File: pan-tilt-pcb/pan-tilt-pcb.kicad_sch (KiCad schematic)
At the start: 23 parts, among them J1 Conn_01x03, J10 USB_C_Receptacle_USB2.0_14P, J2 NC5MAV, J3 NC5FAV, J4 Conn_01x03, J5 Conn_01x03, J6 Conn_01x03, J7 Conn_01x03, J8 Conn_01x12, J9 Conn_01x12, SW1 SW_Push, SW2 SW_Push

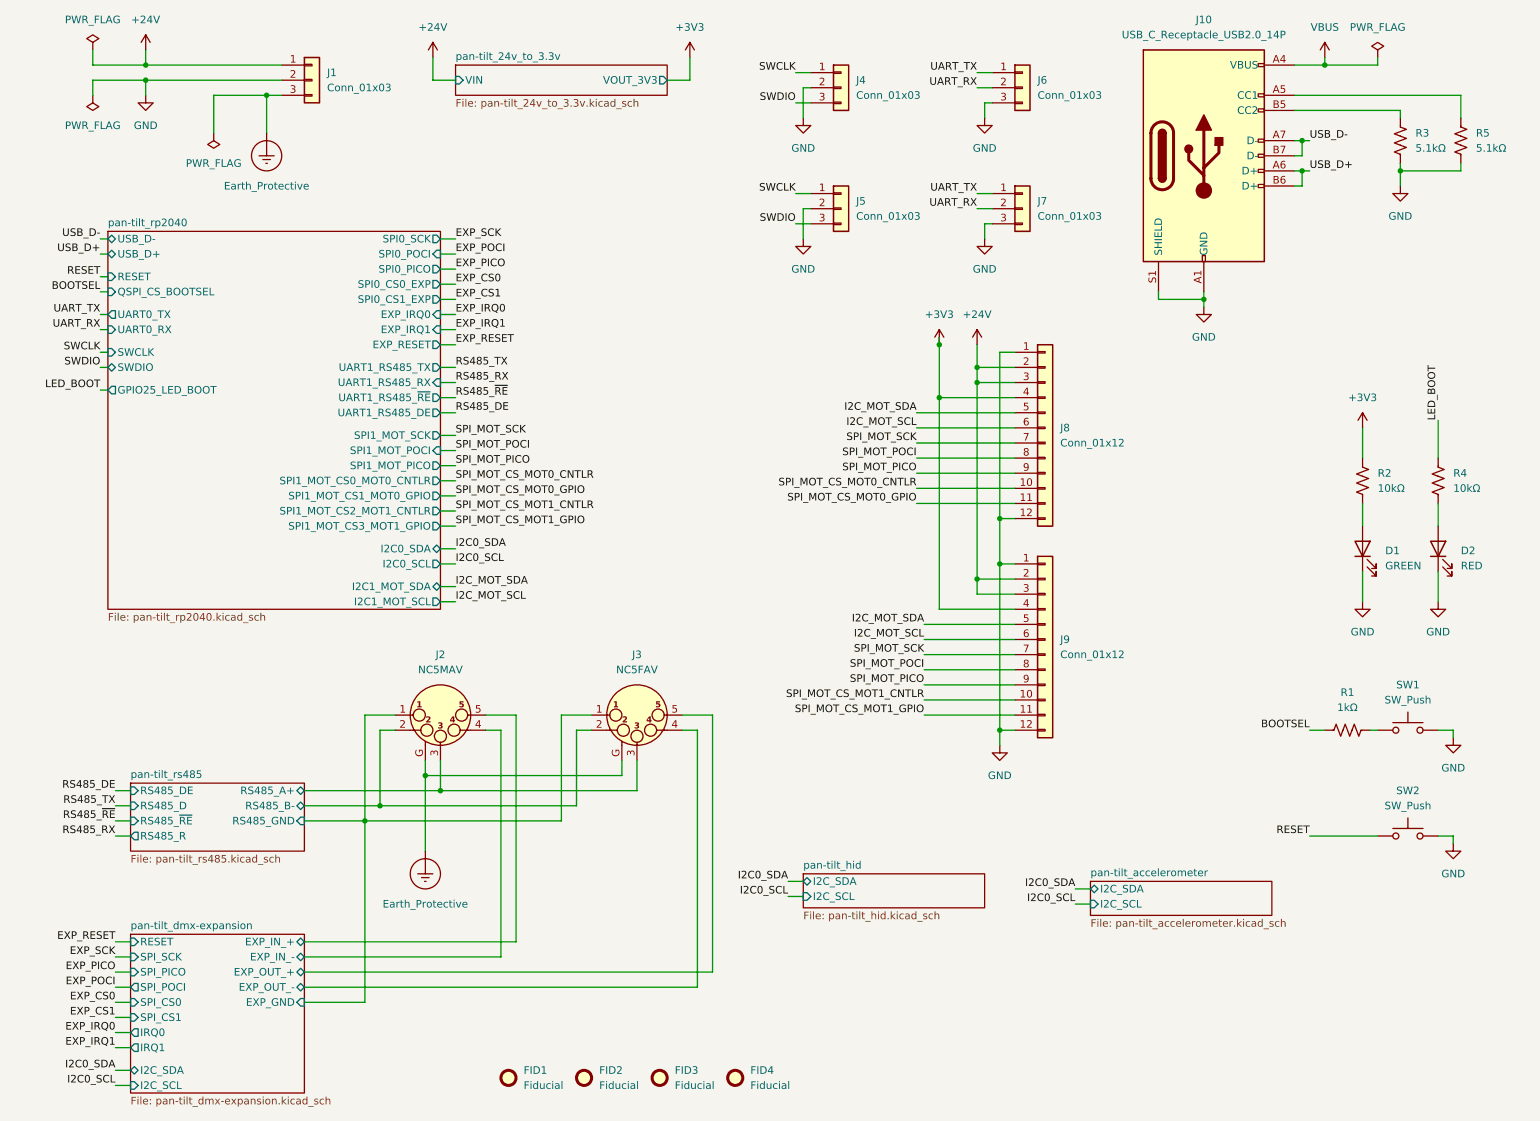
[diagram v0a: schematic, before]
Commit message: fix missing pieces, incorporate review feedback
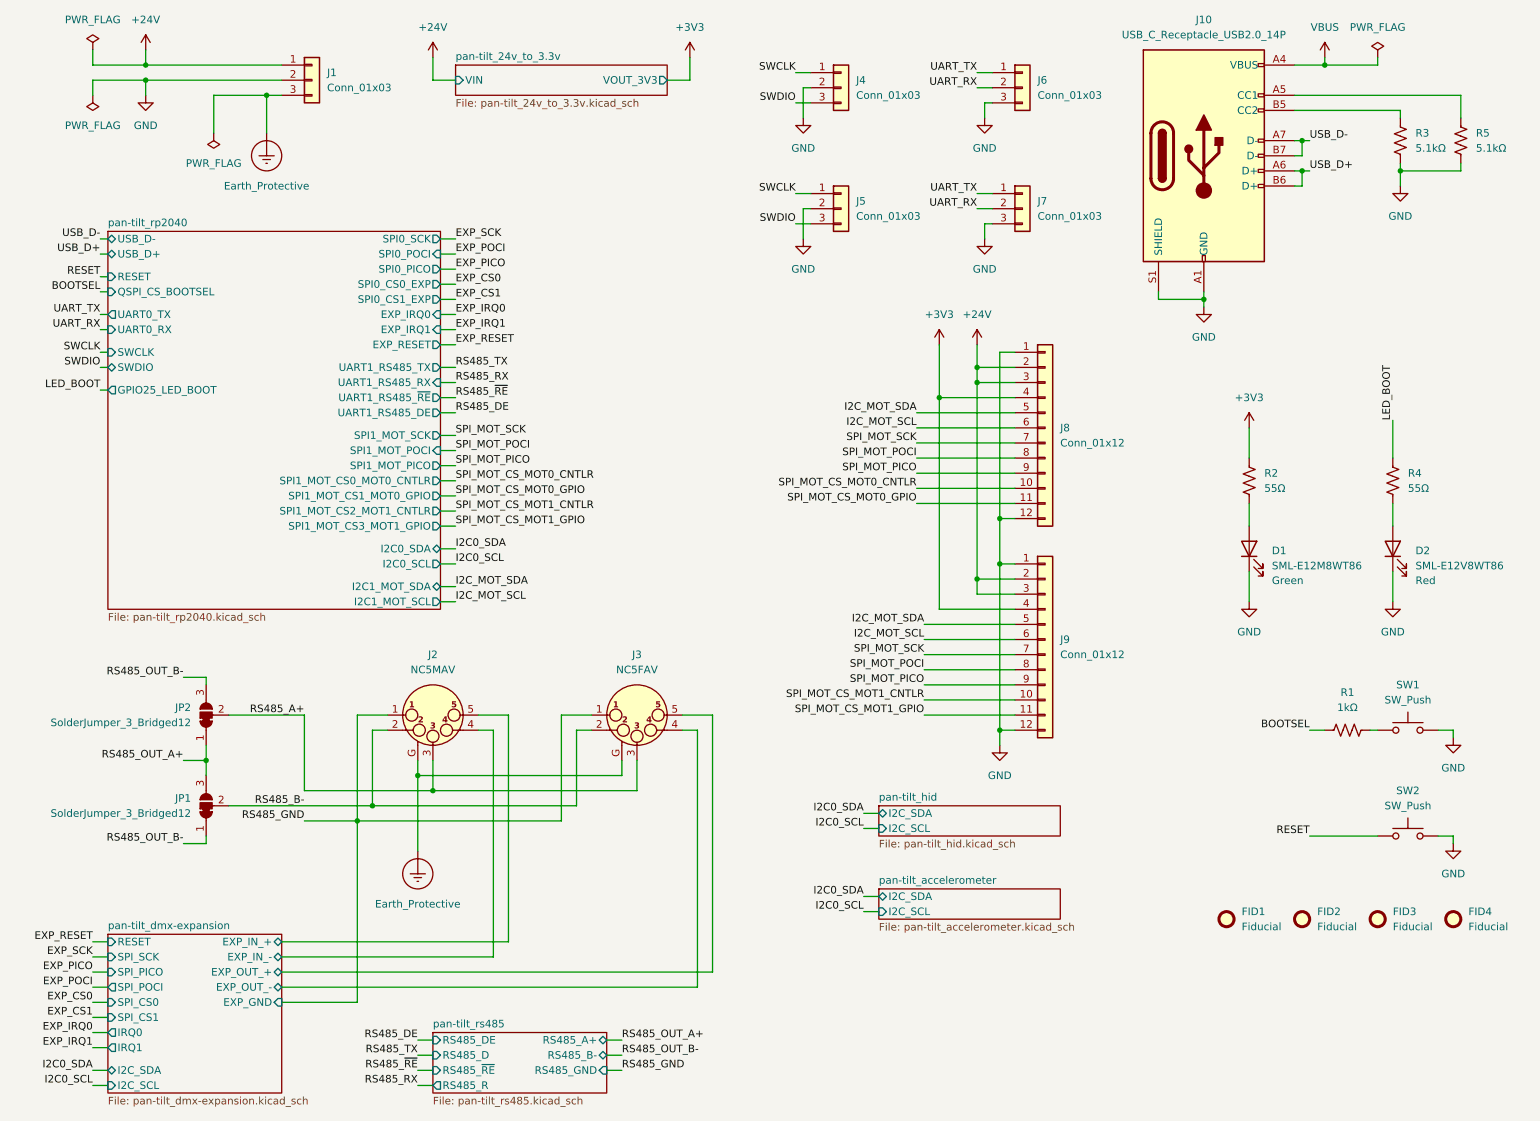
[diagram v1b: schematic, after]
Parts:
- added JP1, JP2: SolderJumper_3_Bridged12, symbol Jumper:SolderJumper_3_Bridged12
- D1: value GREEN -> SML-E12M8WT86; footprint (none) -> LED_SMD:LED_0603_1608Metric; Color (none) -> Green
- D2: value RED -> SML-E12V8WT86; Color (none) -> Red
- R2, R4: value 10kΩ -> 55Ω
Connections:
- net pan-tilt_dmx-expansion/EXP_GND renamed RS485_GND
- net pan-tilt_rs485/RS485_A+ renamed RS485_A+
- net RS485_A+: now also JP2.2 (C)
- net pan-tilt_rs485/RS485_B- renamed RS485_B-
- net RS485_B-: now also JP1.2 (C)
- new net RS485_OUT_A+: JP1.3 (B), JP2.1 (A)
- new net RS485_OUT_B-: JP1.1 (A), JP2.3 (B)
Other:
- moved on the sheet: D1, D2, FID1, FID2, FID3, FID4, J2, R2, R4

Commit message: rename to pan-tilt-pcb everywhere
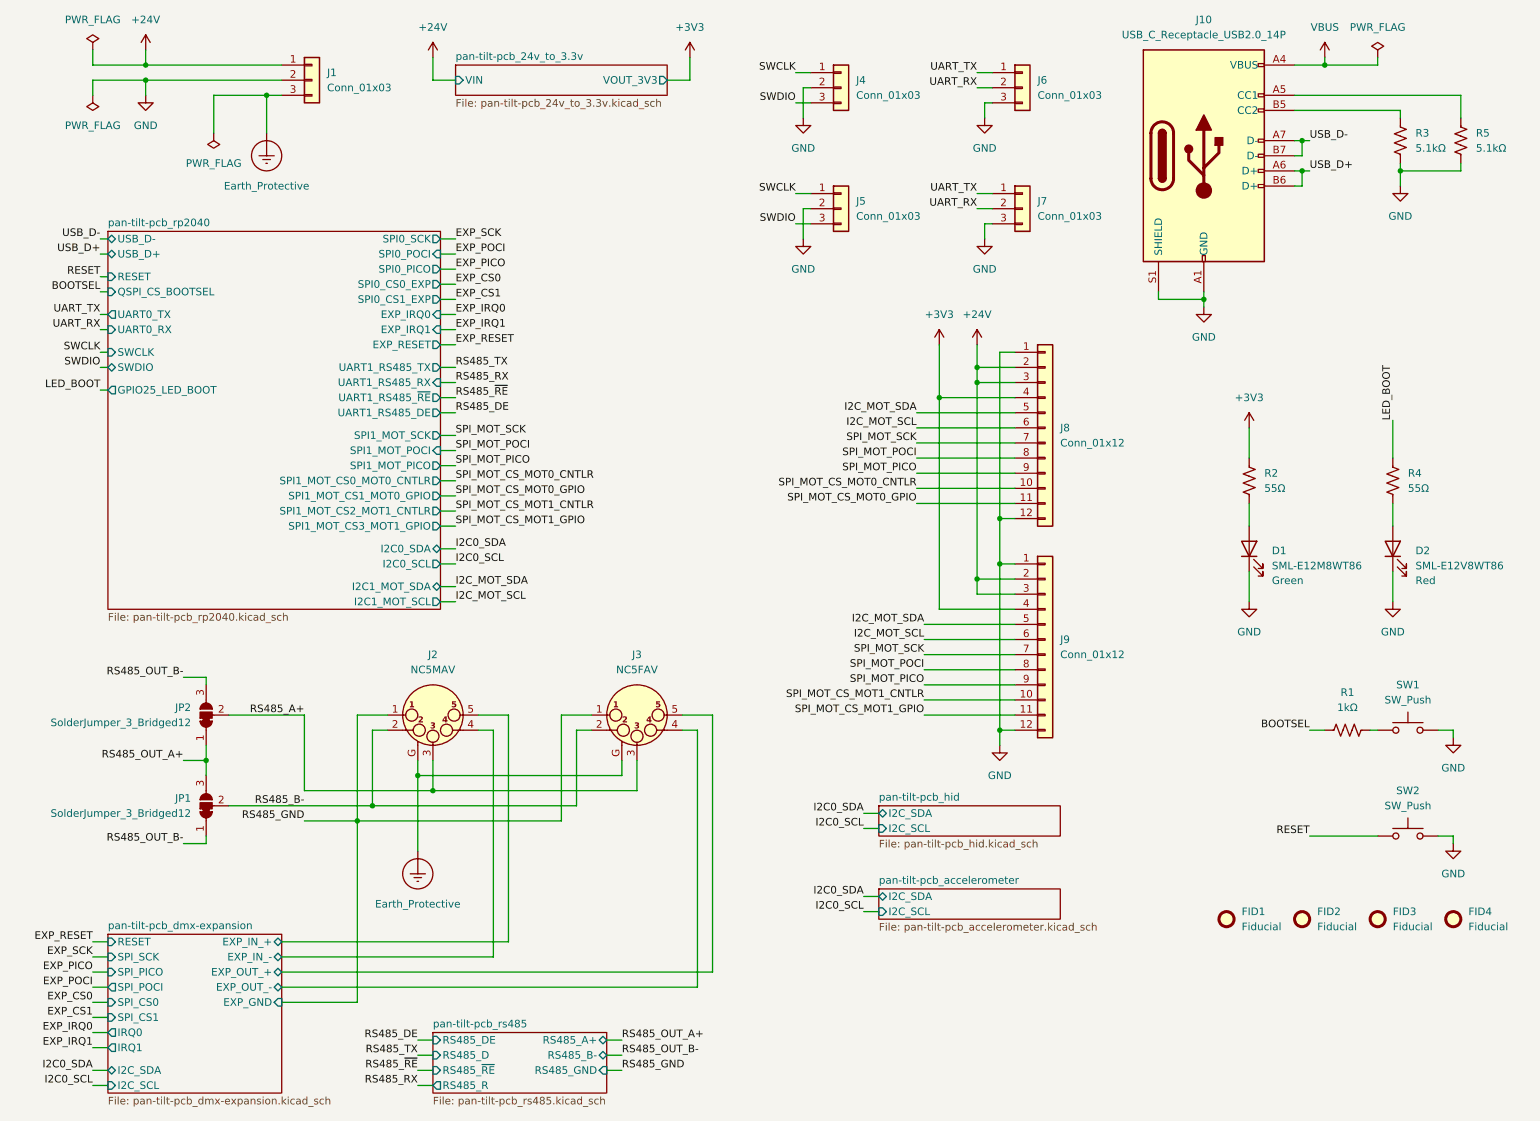
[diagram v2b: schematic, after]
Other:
- sheet pan-tilt_24v_to_3.3v renamed pan-tilt-pcb_24v_to_3.3v
- sheet pan-tilt_accelerometer renamed pan-tilt-pcb_accelerometer
- sheet pan-tilt_dmx-expansion renamed pan-tilt-pcb_dmx-expansion
- sheet pan-tilt_hid renamed pan-tilt-pcb_hid
- sheet pan-tilt_rp2040 renamed pan-tilt-pcb_rp2040
- sheet pan-tilt_rs485 renamed pan-tilt-pcb_rs485
- sheet pan-tilt-pcb_24v_to_3.3v: file pan-tilt_24v_to_3.3v.kicad_sch -> pan-tilt-pcb_24v_to_3.3v.kicad_sch
- sheet pan-tilt-pcb_accelerometer: file pan-tilt_accelerometer.kicad_sch -> pan-tilt-pcb_accelerometer.kicad_sch
- sheet pan-tilt-pcb_dmx-expansion: file pan-tilt_dmx-expansion.kicad_sch -> pan-tilt-pcb_dmx-expansion.kicad_sch
- sheet pan-tilt-pcb_hid: file pan-tilt_hid.kicad_sch -> pan-tilt-pcb_hid.kicad_sch
- sheet pan-tilt-pcb_rp2040: file pan-tilt_rp2040.kicad_sch -> pan-tilt-pcb_rp2040.kicad_sch
- sheet pan-tilt-pcb_rs485: file pan-tilt_rs485.kicad_sch -> pan-tilt-pcb_rs485.kicad_sch
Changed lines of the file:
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@@
 			(color 0 0 0 0.0000)
 		)
-		(property "Sheetname" "pan-tilt_rp2040"
+		(property "Sheetname" "pan-tilt-pcb_rp2040"
 			(at 29.21 50.0884 0)
 			(effects
@@
 			)
 		)
-		(property "Sheetfile" "pan-tilt_rp2040.kicad_sch"
+		(property "Sheetfile" "pan-tilt-pcb_rp2040.kicad_sch"
 			(at 29.21 114.8846 0)
 			(effects
@@
 			(color 0 0 0 0.0000)
 		)
-		(property "Sheetname" "pan-tilt_hid"
+		(property "Sheetname" "pan-tilt-pcb_hid"
 			(at 158.75 146.6084 0)
 			(effects
@@
 			)
 		)
-		(property "Sheetfile" "pan-tilt_hid.kicad_sch"
+		(property "Sheetfile" "pan-tilt-pcb_hid.kicad_sch"
 			(at 158.75 152.9846 0)
 			(effects
@@
 			(color 0 0 0 0.0000)
 		)
-		(property "Sheetname" "pan-tilt_accelerometer"
+		(property "Sheetname" "pan-tilt-pcb_accelerometer"
 			(at 158.75 160.5784 0)
 			(effects
@@
 			)
 		)
-		(property "Sheetfile" "pan-tilt_accelerometer.kicad_sch"
+		(property "Sheetfile" "pan-tilt-pcb_accelerometer.kicad_sch"
 			(at 158.75 166.9546 0)
 			(effects
@@
 			(color 0 0 0 0.0000)
 		)
-		(property "Sheetname" "pan-tilt_rs485"
+		(property "Sheetname" "pan-tilt-pcb_rs485"
 			(at 83.82 184.7084 0)
 			(effects
@@
 			)
 		)
-		(property "Sheetfile" "pan-tilt_rs485.kicad_sch"
+		(property "Sheetfile" "pan-tilt-pcb_rs485.kicad_sch"
 			(at 83.82 196.1646 0)
 			(effects
@@
 			(color 0 0 0 0.0000)
 		)
-		(property "Sheetname" "pan-tilt_24v_to_3.3v"
+		(property "Sheetname" "pan-tilt-pcb_24v_to_3.3v"
 			(at 87.63 22.1484 0)
 			(effects
@@
 			)
 		)
-		(property "Sheetfile" "pan-tilt_24v_to_3.3v.kicad_sch"
+		(property "Sheetfile" "pan-tilt-pcb_24v_to_3.3v.kicad_sch"
 			(at 87.63 28.5246 0)
 			(effects
@@
 			(color 0 0 0 0.0000)
 		)
-		(property "Sheetname" "pan-tilt_dmx-expansion"
+		(property "Sheetname" "pan-tilt-pcb_dmx-expansion"
 			(at 29.21 168.1984 0)
 			(effects
@@
 			)
 		)
-		(property "Sheetfile" "pan-tilt_dmx-expansion.kicad_sch"
+		(property "Sheetfile" "pan-tilt-pcb_dmx-expansion.kicad_sch"
 			(at 29.21 196.1646 0)
 			(effects
